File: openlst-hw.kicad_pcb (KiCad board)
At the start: 4 copper layers, 80 x 80 mm, 165 parts, among them J1 CC Prog/Debug, J10 EXT 5V, J11 EXT VRF, J12 EXT 3V3, J13 MS UART0, J14 MS Prog/Debug, J15 MS UART1, J16 ANT, J17 Switch Select, J18 Conn_Coaxial, J2 UART0, J7 Control Outputs, J8 Conn_02x24_Odd_Even, J9 EXT VBAT, U1 CC1110, U10 PE4250MLI, U11 0433BM15A0001, U12 RFFM6406, U2 MIC803, U3 AP63205WU, U4 AP63203WU, U5 AP63200WU, U6 MSPM0G3107SDGS20R, U7 TJA1051TK-3, U8 SF2446E, U9 PE4250MLI, X1 TG2520SMN 27MHz

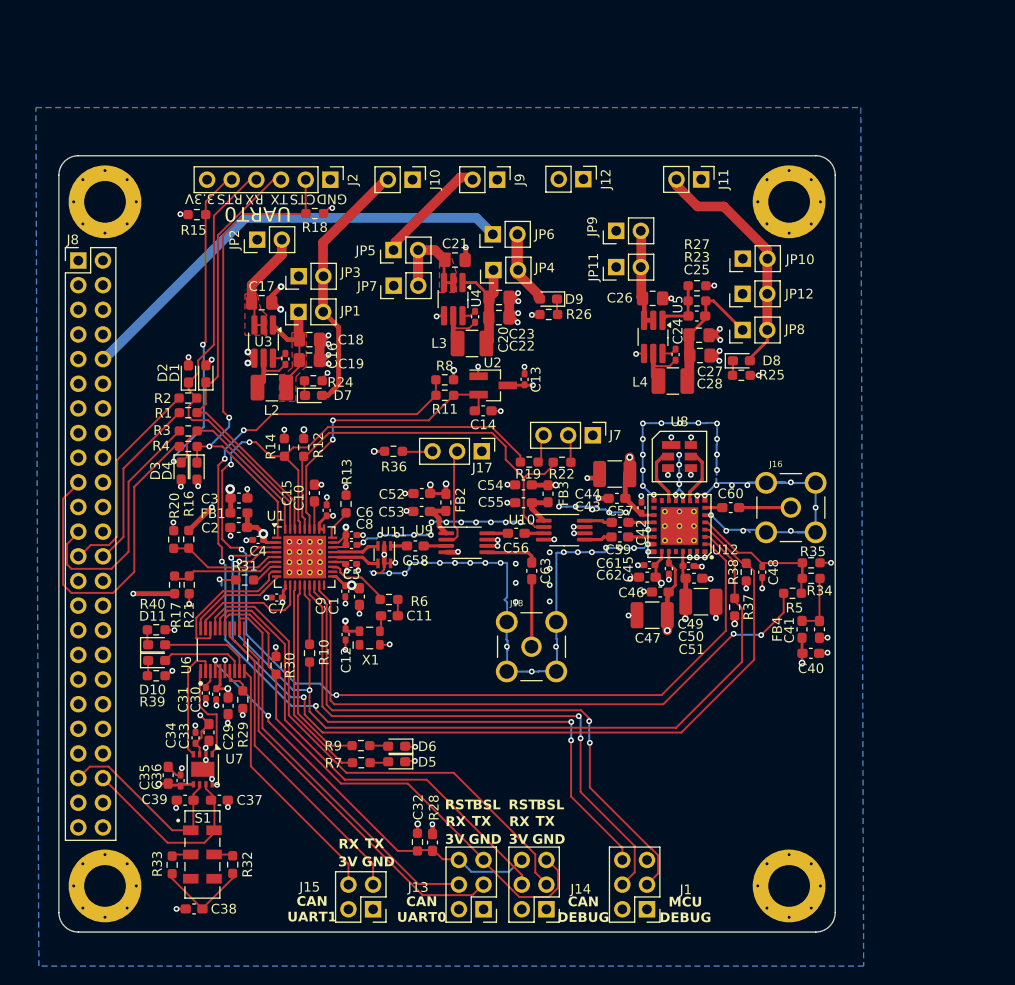
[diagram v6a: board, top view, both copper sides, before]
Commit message: automatic schematic and pcb valiadation and cleanup
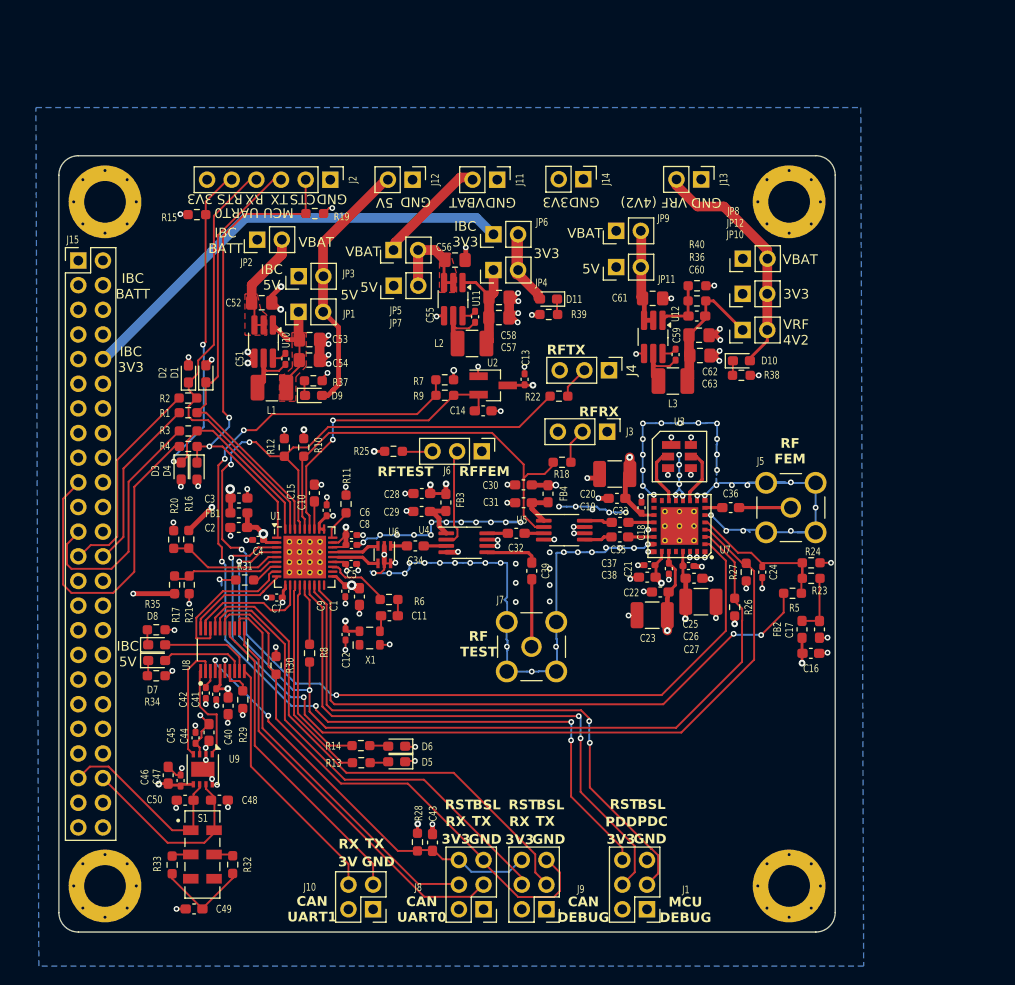
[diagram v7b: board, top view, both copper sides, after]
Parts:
- removed the R19 at (108.5, 91.6)
- added J4: Control Outputs, Connector_PinHeader_2.54mm:PinHeader_1x03_P2.54mm_Vertical, F.Cu at (116.7, 82.1)
- added R22: 22, Resistor_SMD:R_0603_1608Metric_Pad0.98x0.95mm_HandSolder, F.Cu at (111.5, 84.8)
- moved J3 1.53 mm to (116.5, 88.4)
- moved JP6 0.06 mm to (104.8, 68.1)
- renumbered C40 to C16, C41 to C17, C42 to C18, C43 to C19, C44 to C20, C45 to C21, C46 to C22, C47 to C23, C48 to C24, C49 to C25, C50 to C26, C51 to C27, C52 to C28, C53 to C29, C54 to C30, C55 to C31, C56 to C32, C57 to C33, C58 to C34, C59 to C35, C60 to C36, C61 to C37, C62 to C38, C63 to C39, C29 to C40, C30 to C41, C31 to C42, C32 to C43, C33 to C44, C34 to C45, C35 to C46, C36 to C47, C37 to C48, C38 to C49, C39 to C50, C16 to C51, C17 to C52, C18 to C53, C19 to C54, C20 to C55, C21 to C56, C22 to C57, C23 to C58, C24 to C59, C25 to C60, C26 to C61, C27 to C62, C28 to C63, D8 to D10, D9 to D11, D10 to D7, D11 to D8, D7 to D9, FB4 to FB2, FB2 to FB3, FB3 to FB4, J15 to J10, J9 to J11, J10 to J12, J11 to J13, J12 to J14, J8 to J15, J7 to J3, J16 to J5, J17 to J6, J18 to J7, J13 to J8, J14 to J9, L2 to L1, L3 to L2, L4 to L3, R12 to R10, R13 to R11, R14 to R12, R7 to R13, R9 to R14, R22 to R18, R18 to R19, R34 to R23, R35 to R24, R36 to R25, R37 to R26, R38 to R27, R39 to R34, R40 to R35, R23 to R36, R24 to R37, R25 to R38, R26 to R39, R27 to R40, R8 to R7, R10 to R8, R11 to R9, U3 to U10, U4 to U11, U5 to U12, U8 to U3, U9 to U4, U10 to U5, U11 to U6, U12 to U7, U6 to U8, U7 to U9
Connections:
- J3 pad 3: Net-(J7-Pin_3) -> +3V3
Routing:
- net Net-(J4-Pin_2): track 0.00 -> 3.38 mm
- net Net-(J7-Pin_3): track 2.99 -> 0.00 mm
- net LST_TX_MODE: track 127.9 -> 130.4 mm
- net Net-(J3-Pin_2): track 2.90 -> 3.67 mm
- net /UART-CAN/BSL: track 56.2 -> 56.7 mm
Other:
- board text added: "3V3"
- board text added: "5V"
- board text added: "IBC 3V3"
- board text added: "IBC 5V"
- board text added: "IBC BATT"
- board text added: "MCU UART0"
- board text added: "PDC"
- board text added: "PDD"
- board text added: "RF FEM"
- board text added: "RF TEST"
- board text added: "RFFEM"
- board text added: "RFRX"
- board text added: "RFTEST"
- board text added: "RFTX"
- board text added: "VBAT"
- board text added: "VRF (4V2)"
- board text added: "VRF 4V2"
- board text removed: "3.3V"
- board text removed: "UART0"
